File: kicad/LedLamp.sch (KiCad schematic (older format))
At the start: 16 parts, among them J1 RGB+Vcc, J2 Bornier, Q1 IRF540N, Q2 IRF540N, Q3 IRF540N, SW1 button, U1 ATmega328P-PU

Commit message: Removed pull-down for mosfet gates
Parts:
- removed C1: 1u, Capacitor_THT:CP_Radial_D4.0mm_P2.00mm, symbol Device:CP1_Small
- removed R1, R2, R3: 1k, Resistor_THT:R_Axial_DIN0207_L6.3mm_D2.5mm_P10.16mm_Horizontal, symbol Device:R
- removed R5: R, Resistor_THT:R_Axial_DIN0207_L6.3mm_D2.5mm_P10.16mm_Horizontal, symbol Device:R
- added C1: 0.1u, symbol Device:C
- added R4: 1k, symbol Device:R
- R6: value R -> 10k
- U1: symbol MCU_Microchip_ATmega:ATmega328P-PU -> LedLamp-rescue:ATmega328P-PU-MCU_Microchip_ATmega
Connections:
- wire segments 52 -> 42
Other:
- note added: "Button debouncer"
- moved on the sheet: R6, SW1
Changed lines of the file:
@@
 EESchema Schematic File Version 4
+LIBS:LedLamp-cache
 EELAYER 26 0
 EELAYER END
@@
 $EndComp
 $Comp
-L MCU_Microchip_ATmega:ATmega328P-PU U1
+L LedLamp-rescue:ATmega328P-PU-MCU_Microchip_ATmega U1
 U 1 1 5BD6257B
 P 3850 4050
@@
 $EndComp
 $Comp
-L Device:R R1
-U 1 1 5BD629AC
-P 2950 2350
-F 0 "R1" V 2743 2350 50  0000 C CNN
-F 1 "1k" V 2834 2350 50  0000 C CNN
-F 2 "Resistor_THT:R_Axial_DIN0207_L6.3mm_D2.5mm_P10.16mm_Horizontal" V 2880 2350 50  0001 C CNN
-F 3 "~" H 2950 2350 50  0001 C CNN
-	1    2950 2350
-	0    1    1    0
-$EndComp
-$Comp
-L Device:R R3
-U 1 1 5BD62AB6
-P 4600 2350
-F 0 "R3" V 4393 2350 50  0000 C CNN
-F 1 "1k" V 4484 2350 50  0000 C CNN
-F 2 "Resistor_THT:R_Axial_DIN0207_L6.3mm_D2.5mm_P10.16mm_Horizontal" V 4530 2350 50  0001 C CNN
-F 3 "~" H 4600 2350 50  0001 C CNN
-	1    4600 2350
-	0    1    1    0
-$EndComp
-$Comp
-L Device:R R2
-U 1 1 5BD62B4E
-P 3700 2350
-F 0 "R2" V 3493 2350 50  0000 C CNN
-F 1 "1k" V 3584 2350 50  0000 C CNN
-F 2 "Resistor_THT:R_Axial_DIN0207_L6.3mm_D2.5mm_P10.16mm_Horizontal" V 3630 2350 50  0001 C CNN
-F 3 "~" H 3700 2350 50  0001 C CNN
-	1    3700 2350
-	0    1    1    0
-$EndComp
-$Comp
 L Switch:SW_Push SW1
 U 1 1 5BD62CB3
-P 6250 2650
-F 0 "SW1" H 6250 2935 50  0000 C CNN
-F 1 "button" H 6250 2844 50  0000 C CNN
-F 2 "Button_Switch_THT:SW_PUSH_6mm_H5mm" H 6250 2850 50  0001 C CNN
-F 3 "" H 6250 2850 50  0001 C CNN
-	1    6250 2650
-	1    0    0    -1
-$EndComp
-$Comp
-L Device:CP1_Small C1
-U 1 1 5BD62E04
-P 6250 2850
-F 0 "C1" V 6022 2850 50  0000 C CNN
-F 1 "1u" V 6113 2850 50  0000 C CNN
-F 2 "Capacitor_THT:CP_Radial_D4.0mm_P2.00mm" H 6250 2850 50  0001 C CNN
-F 3 "~" H 6250 2850 50  0001 C CNN
-	1    6250 2850
-	0    1    1    0
+P 6750 2250
+F 0 "SW1" H 6750 2535 50  0000 C CNN
+F 1 "button" H 6750 2444 50  0000 C CNN
+F 2 "Button_Switch_THT:SW_PUSH_6mm_H5mm" H 6750 2450 50  0001 C CNN
+F 3 "" H 6750 2450 50  0001 C CNN
+	1    6750 2250
+	1    0    0    -1
 $EndComp
 Wire Wire Line
@@
 Wire Wire Line
 	4350 3000 4300 3000
-Text Label 5750 2500 0    50   ~ 0
+Text Label 7400 1900 0    50   ~ 0
 Button
-Wire Wire Line
-	5750 2500 5750 2650
-Wire Wire Line
-	5750 2650 5900 2650
-Wire Wire Line
-	6150 2850 6050 2850
-Wire Wire Line
-	6050 2850 6050 2650
-Connection ~ 6050 2650
-Wire Wire Line
-	6350 2850 6450 2850
-Wire Wire Line
-	6450 2850 6450 2650
 $Comp
 L power:VCC #PWR0104
 U 1 1 5BD6723A
-P 7150 2650
-F 0 "#PWR0104" H 7150 2500 50  0001 C CNN
-F 1 "VCC" H 7167 2823 50  0000 C CNN
-F 2 "" H 7150 2650 50  0001 C CNN
-F 3 "" H 7150 2650 50  0001 C CNN
-	1    7150 2650
-	1    0    0    -1
-$EndComp
-$Comp
-L Device:R R5
-U 1 1 5BD67CA0
-P 5900 3050
-F 0 "R5" H 5970 3096 50  0000 L CNN
-F 1 "R" H 5970 3005 50  0000 L CNN
-F 2 "Resistor_THT:R_Axial_DIN0207_L6.3mm_D2.5mm_P10.16mm_Horizontal" V 5830 3050 50  0001 C CNN
-F 3 "~" H 5900 3050 50  0001 C CNN
-	1    5900 3050
-	1    0    0    -1
-$EndComp
-$Comp
-L power:GND #PWR0105
-U 1 1 5BD67E1D
-P 5900 3300
-F 0 "#PWR0105" H 5900 3050 50  0001 C CNN
-F 1 "GND" H 5905 3127 50  0000 C CNN
-F 2 "" H 5900 3300 50  0001 C CNN
-F 3 "" H 5900 3300 50  0001 C CNN
-	1    5900 3300
-	1    0    0    -1
-$EndComp
-Wire Wire Line
-	5900 3300 5900 3200
-Wire Wire Line
-	5900 2900 5900 2650
-Connection ~ 5900 2650
-Wire Wire Line
-	5900 2650 6050 2650
-$Comp
-L Device:R R6
-U 1 1 5BD68949
-P 6750 2650
-F 0 "R6" V 6543 2650 50  0000 C CNN
-F 1 "R" V 6634 2650 50  0000 C CNN
-F 2 "Resistor_THT:R_Axial_DIN0207_L6.3mm_D2.5mm_P10.16mm_Horizontal" V 6680 2650 50  0001 C CNN
-F 3 "~" H 6750 2650 50  0001 C CNN
-	1    6750 2650
-	0    1    1    0
-$EndComp
-Wire Wire Line
-	6450 2650 6600 2650
-Connection ~ 6450 2650
-Wire Wire Line
-	6900 2650 7150 2650
+P 8050 2250
+F 0 "#PWR0104" H 8050 2100 50  0001 C CNN
+F 1 "VCC" H 8067 2423 50  0000 C CNN
+F 2 "" H 8050 2250 50  0001 C CNN
+F 3 "" H 8050 2250 50  0001 C CNN
+	1    8050 2250
+	1    0    0    -1
+$EndComp
+Connection ~ 7400 2250
 $Comp
 L power:VCC #PWR0106
@@
 Wire Wire Line
 	1750 1350 1750 1450
-Wire Wire Line
-	4750 2550 4750 2350
-Wire Wire Line
-	4750 2200 4750 2350
-Connection ~ 4750 2350
-Wire Wire Line
-	3850 2200 3850 2350
-Connection ~ 3850 2350
-Wire Wire Line
-	3850 2350 3850 2650
-Connection ~ 3100 2350
-Wire Wire Line
-	3100 2350 3100 2200
-Wire Wire Line
-	3100 2350 3100 2700
-$Comp
-L power:GND #PWR0109
-U 1 1 5BD72FEA
-P 2700 2350
-F 0 "#PWR0109" H 2700 2100 50  0001 C CNN
-F 1 "GND" H 2705 2177 50  0000 C CNN
-F 2 "" H 2700 2350 50  0001 C CNN
-F 3 "" H 2700 2350 50  0001 C CNN
-	1    2700 2350
-	1    0    0    -1
-$EndComp
-$Comp
-L power:GND #PWR0110
-U 1 1 5BD7302A
-P 3500 2350
-F 0 "#PWR0110" H 3500 2100 50  0001 C CNN
-F 1 "GND" H 3505 2177 50  0000 C CNN
-F 2 "" H 3500 2350 50  0001 C CNN
-F 3 "" H 3500 2350 50  0001 C CNN
-	1    3500 2350
-	1    0    0    -1
-$EndComp
-$Comp
-L power:GND #PWR0111
-U 1 1 5BD7306A
-P 4400 2350
-F 0 "#PWR0111" H 4400 2100 50  0001 C CNN
-F 1 "GND" H 4405 2177 50  0000 C CNN
-F 2 "" H 4400 2350 50  0001 C CNN
-F 3 "" H 4400 2350 50  0001 C CNN
-	1    4400 2350
-	1    0    0    -1
-$EndComp
-Wire Wire Line
-	2700 2350 2800 2350
-Wire Wire Line
-	3500 2350 3550 2350
-Wire Wire Line
-	4400 2350 4450 2350
 $Comp
 L Connector:Screw_Terminal_01x02 J2
@@
 Wire Wire Line
 	800  2200 1000 2200
+Wire Wire Line
+	7800 2250 8050 2250
+Wire Wire Line
+	7350 2250 7400 2250
+$Comp
+L Device:R R6
+U 1 1 5BD68949
+P 7650 2250
+F 0 "R6" V 7650 2250 50  0000 C CNN
+F 1 "10k" V 7534 2250 50  0000 C CNN
+F 2 "Resistor_THT:R_Axial_DIN0207_L6.3mm_D2.5mm_P10.16mm_Horizontal" V 7580 2250 50  0001 C CNN
+F 3 "~" H 7650 2250 50  0001 C CNN
+	1    7650 2250
+	0    1    1    0
+$EndComp
+$Comp
+L Device:R R4
+U 1 1 5BDCECC9
+P 7200 2250
+F 0 "R4" V 7200 2250 50  0000 C CNN
+F 1 "1k" V 7084 2250 50  0000 C CNN
+F 2 "" V 7130 2250 50  0001 C CNN
+F 3 "~" H 7200 2250 50  0001 C CNN
+	1    7200 2250
+	0    1    1    0
+$EndComp
+Wire Wire Line
+	7050 2250 6950 2250
+Wire Wire Line
+	7400 2250 7400 1900
+$Comp
+L power:GND #PWR01
+U 1 1 5BDD1639
+P 6550 2450
+F 0 "#PWR01" H 6550 2200 50  0001 C CNN
+F 1 "GND" H 6555 2277 50  0000 C CNN
+F 2 "" H 6550 2450 50  0001 C CNN
+F 3 "" H 6550 2450 50  0001 C CNN
+	1    6550 2450
+	1    0    0    -1
+$EndComp
+Wire Wire Line
+	6550 2250 6550 2450
+$Comp
+L Device:C C1
+U 1 1 5BDD1FB2
+P 7400 2450
+F 0 "C1" H 7515 2496 50  0000 L CNN
+F 1 "0.1u" H 7515 2405 50  0000 L CNN
+F 2 "" H 7438 2300 50  0001 C CNN
+F 3 "~" H 7400 2450 50  0001 C CNN
+	1    7400 2450
+	1    0    0    -1
+$EndComp
+Wire Wire Line
+	7400 2250 7500 2250
+Wire Wire Line
+	7400 2250 7400 2300
+$Comp
+L power:GND #PWR02
+U 1 1 5BDD3565
+P 7400 2600
+F 0 "#PWR02" H 7400 2350 50  0001 C CNN
+F 1 "GND" H 7405 2427 50  0000 C CNN
+F 2 "" H 7400 2600 50  0001 C CNN
+F 3 "" H 7400 2600 50  0001 C CNN
+	1    7400 2600
+	1    0    0    -1
+$EndComp
+Wire Notes Line
+	6300 1550 8350 1550
+Wire Notes Line
+	8350 1550 8350 3000
+Wire Notes Line
+	8350 3000 6300 3000
+Text Notes 7650 2950 0    50   ~ 0
+Button debouncer
+Wire Notes Line
+	6300 1550 6300 3000
+Wire Wire Line
+	3100 2200 3100 2700
+Wire Wire Line
+	3850 2200 3850 2650
+Wire Wire Line
+	4750 2200 4750 2550
 $EndSCHEMATC

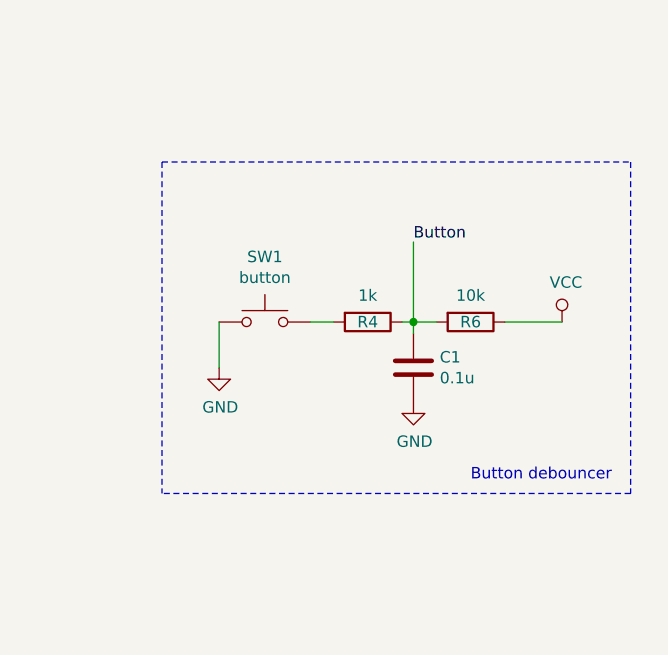
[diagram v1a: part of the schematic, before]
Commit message: Now use LOW level on INT0
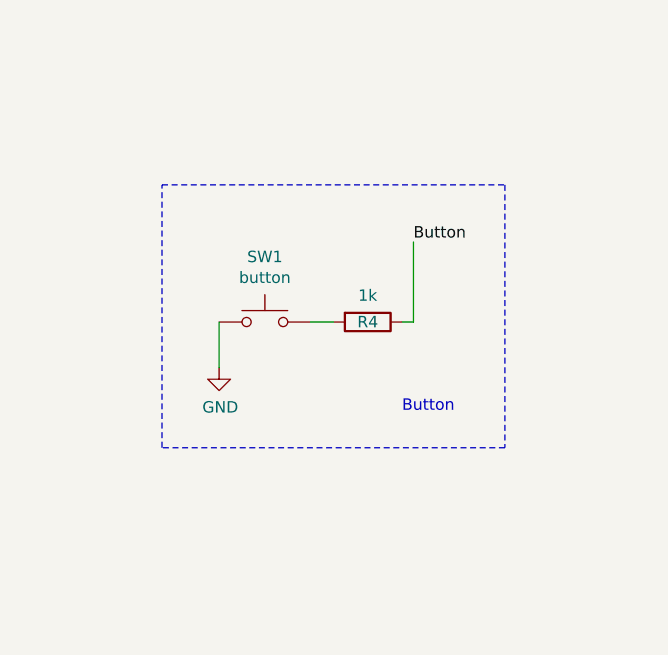
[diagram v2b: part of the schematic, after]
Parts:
- removed C1: 0.1u, symbol Device:C
- removed R6: 10k, Resistor_THT:R_Axial_DIN0207_L6.3mm_D2.5mm_P10.16mm_Horizontal, symbol Device:R
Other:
- note added: "Button"
- note removed: "Button debouncer"
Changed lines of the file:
@@
 Button
-$Comp
-L power:VCC #PWR0104
-U 1 1 5BD6723A
-P 8050 2250
-F 0 "#PWR0104" H 8050 2100 50  0001 C CNN
-F 1 "VCC" H 8067 2423 50  0000 C CNN
-F 2 "" H 8050 2250 50  0001 C CNN
-F 3 "" H 8050 2250 50  0001 C CNN
-	1    8050 2250
-	1    0    0    -1
-$EndComp
-Connection ~ 7400 2250
 $Comp
 L power:VCC #PWR0106
@@
 	800  2200 1000 2200
 Wire Wire Line
-	7800 2250 8050 2250
-Wire Wire Line
 	7350 2250 7400 2250
-$Comp
-L Device:R R6
-U 1 1 5BD68949
-P 7650 2250
-F 0 "R6" V 7650 2250 50  0000 C CNN
-F 1 "10k" V 7534 2250 50  0000 C CNN
-F 2 "Resistor_THT:R_Axial_DIN0207_L6.3mm_D2.5mm_P10.16mm_Horizontal" V 7580 2250 50  0001 C CNN
-F 3 "~" H 7650 2250 50  0001 C CNN
-	1    7650 2250
-	0    1    1    0
-$EndComp
 $Comp
 L Device:R R4
@@
 Wire Wire Line
 	6550 2250 6550 2450
-$Comp
-L Device:C C1
-U 1 1 5BDD1FB2
-P 7400 2450
-F 0 "C1" H 7515 2496 50  0000 L CNN
-F 1 "0.1u" H 7515 2405 50  0000 L CNN
-F 2 "" H 7438 2300 50  0001 C CNN
-F 3 "~" H 7400 2450 50  0001 C CNN
-	1    7400 2450
-	1    0    0    -1
-$EndComp
-Wire Wire Line
-	7400 2250 7500 2250
-Wire Wire Line
-	7400 2250 7400 2300
-$Comp
-L power:GND #PWR02
-U 1 1 5BDD3565
-P 7400 2600
-F 0 "#PWR02" H 7400 2350 50  0001 C CNN
-F 1 "GND" H 7405 2427 50  0000 C CNN
-F 2 "" H 7400 2600 50  0001 C CNN
-F 3 "" H 7400 2600 50  0001 C CNN
-	1    7400 2600
-	1    0    0    -1
-$EndComp
-Wire Notes Line
-	6300 1550 8350 1550
-Wire Notes Line
-	8350 1550 8350 3000
-Wire Notes Line
-	8350 3000 6300 3000
-Text Notes 7650 2950 0    50   ~ 0
-Button debouncer
-Wire Notes Line
-	6300 1550 6300 3000
+Text Notes 7350 2650 0    50   ~ 0
+Button
 Wire Wire Line
 	3100 2200 3100 2700
@@
 Wire Wire Line
 	4750 2200 4750 2550
+Wire Notes Line
+	7800 1650 7800 2800
+Wire Notes Line
+	7800 2800 6300 2800
+Wire Notes Line
+	6300 2800 6300 1650
+Wire Notes Line
+	6300 1650 7800 1650
 $EndSCHEMATC
